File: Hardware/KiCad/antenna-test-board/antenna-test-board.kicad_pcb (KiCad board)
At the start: 2 copper layers, 50 x 80 mm, 3 parts, among them J1 50R

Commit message: chore(hardware): .kicad_pcb canonico, build reproducible byte a byte
Los UUID deterministas del commit anterior no bastaban: al guardar, KiCad
ordena footprints, pistas, vias y zonas con un criterio que acaba dependiendo
de sus KIID aleatorios, y reordena tambien los fp_text DENTRO de cada
footprint. El orden de los bloques cambiaba en cada build.

canonicalize() reordena los dos niveles por (tipo, texto sin UUID), que no
depende de nada aleatorio, preservando la indentacion que escribe KiCad. El
orden de los hijos de una s-expresion no tiene significado semantico, y
verify_board.py recarga el archivo y corre el DRC justo despues.

Comprobado con tres build.sh seguidos: mismo MD5 del .kicad_pcb las tres
veces, y DRC sigue en 0. Ahora un diff en un fichero generado significa un
cambio real de geometria.

Co-Authored-By: Claude Opus 5 <noreply@anthropic.com>
Claude-Session: https://claude.ai/code/session_01MCMeByymMLU6SJT81sefdN
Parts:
- removed the C101 at (39.2, 26.4)
- added J1: 50R, 0G_RF:TP_Coax_50R_NanoVNA, F.Cu at (39.2, 30.5)
- C101: renamed from J1; value 50R -> 2.2pF; footprint 0G_RF:TP_Coax_50R_NanoVNA -> 0G_RF:C_0402_1005Metric_0G
- moved C101 4.09 mm to (39.2, 26.4), turned to -90 degrees
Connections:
- C101 pad 1: GND -> ANT_FEED

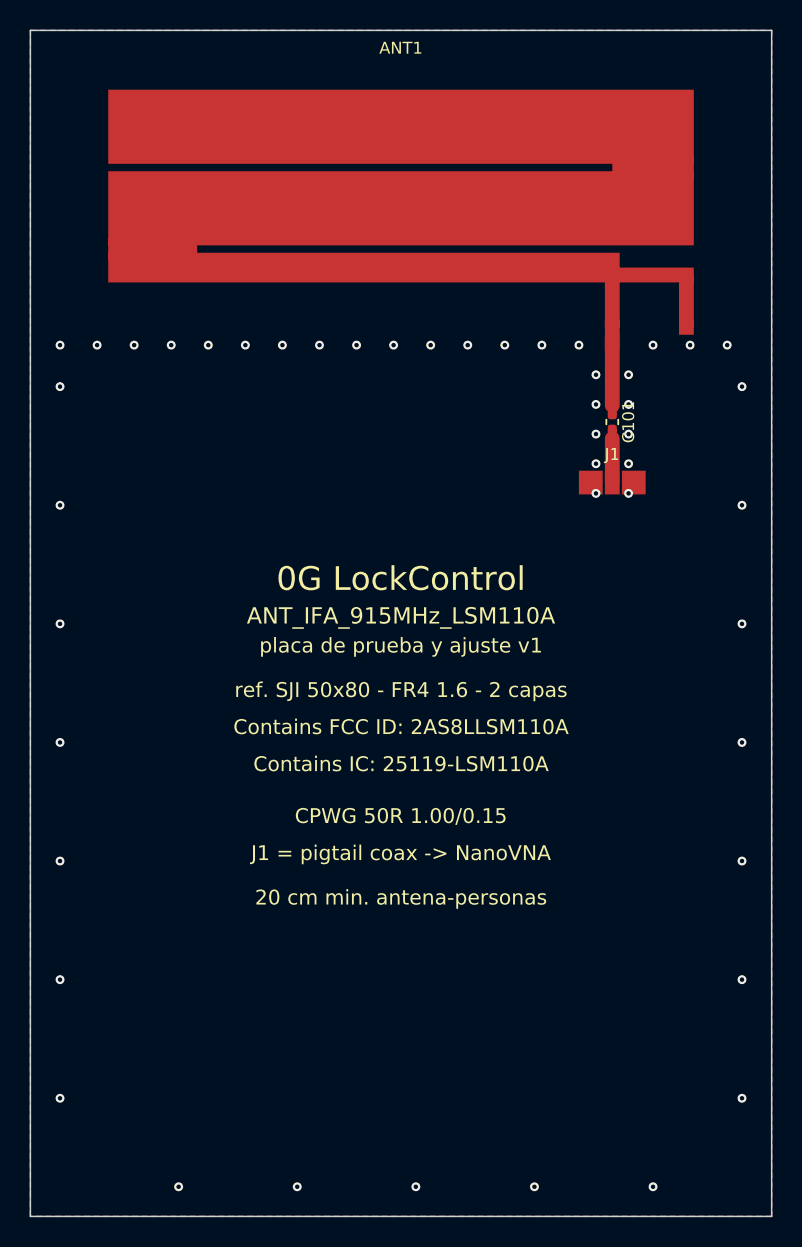
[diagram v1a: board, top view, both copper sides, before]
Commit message: feat(hardware): red de matching en PI segun la figura EVM LSM de SJI
La figura de la placa de evaluacion muestra junto al feed de la antena cuatro
designadores: CON101 (conector RF), L101, C101 y C102. O sea que la referencia
no lleva un condensador suelto en serie, lleva una red en PI con una posicion
serie y dos shunt. Eso resuelve la discrepancia que quedaba abierta entre el
plano ('C101 en serie') y certificacion-FCC/README.md ('C101 shunt'): las dos
fuentes describen la misma red, el plano la resume por un componente.

La placa de prueba pasa a montar las tres posiciones, con la poblacion de
referencia del User Manual FCC como valores por defecto (L101 = 0R, C101 =
2.2 pF, C102 = DNI). Asi se puede realizar cualquier topologia al ajustar
-serie sola, L, PI- sin rehacer la placa.

Detalles de layout que importan en RF:
- El pad interior de cada shunt monta SOBRE la linea (0.45 mm de solape). Con
  un muñon de 1 o 2 mm su inductancia serie arruinaria justo lo que el
  condensador tiene que hacer.
- Cada pad de GND de shunt lleva una via de retorno pegada (0.00 mm).
- La costura de vias esquiva los footprints: una via sobre un pad de GND no
  daria error de DRC (misma red), quedaria sin marcar y mal.
- El componente serie queda donde el plano pone la cota de 5.60.

Cotejo independiente de la geometria contra la misma figura, escalando por el
contorno de 50 x 80 mm del User Manual: las siete cotas medibles cuadran, y el
lado corto de la antena sale a 13.01 mm frente a los 13.00 de la
reconstruccion. La figura corrobora tambien la fila de ranuras mecanicas
(18.5 mm del borde, 1.95 de ancho), que pasa de 'sin verificar' a 'real pero
sin cotar': se mantiene en footprint aparte porque lo que falta es su cota.

Verificacion: 122 comprobaciones (17 + 63 + 42), 0 fallos, DRC en 0. Dos
errores nuevos encontrados y corregidos: serigrafias de C102 y J1 solapadas, y
el punto de sondeo del gap coplanar que caia sobre un pad de C101 y media
0.276 en vez de 0.15.

Queda abierto: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
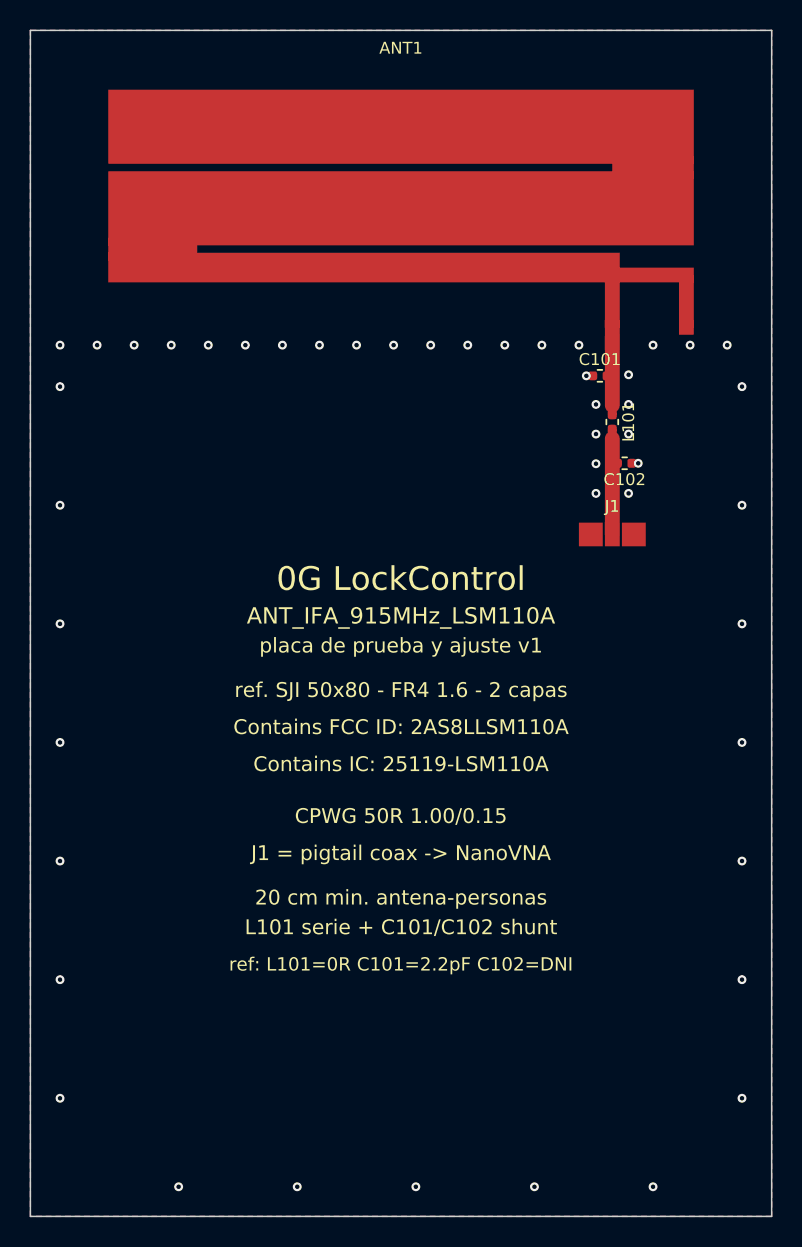
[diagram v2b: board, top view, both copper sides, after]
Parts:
- added C102: DNI, 0G_RF:C_0402_1005Metric_0G, F.Cu at (40.1, 29.2)
- added J1: 50R, 0G_RF:TP_Coax_50R_NanoVNA, F.Cu at (39.2, 34.0)
- L101: renamed from J1; value 50R -> 0R; footprint 0G_RF:TP_Coax_50R_NanoVNA -> 0G_RF:C_0402_1005Metric_0G
- moved L101 4.09 mm to (39.2, 26.4), turned to -90 degrees
- moved C101 3.22 mm to (38.4, 23.3), turned to 0 degrees
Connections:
- C101 pad 1: ANT_FEED -> GND
- C101 pad 2: RF_IN -> ANT_FEED
- L101 pad 1: GND -> ANT_FEED
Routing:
- net RF_IN: track 3.60 -> 7.10 mm
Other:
- board text added: "L101 serie + C101/C102 shunt"
- board text added: "ref: L101=0R C101=2.2pF C102=DNI"
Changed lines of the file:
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@@
+)
+  (footprint "0G_RF:C_0402_1005Metric_0G" (layer "F.Cu")
+    (at 38.415 23.3)
+    (descr "Condensador 0402 (1005 metrico), land IPC nominal: 2 pads de 0.60 x 0.60 mm a +/-0.485 mm. Definido en el proyecto para no depender de las bibliotecas estandar de KiCad. Uso previsto: C101, condensador serie de acoplo/matching en la linea RF de la antena.")
+    (tags "capacitor 0402 1005 RF matching")
+    (attr smd)
+    (fp_text reference "C101" (at 0 -1.1) (layer "F.SilkS")
+        (effects (font (size 0.8 0.8) (thickness 0.12)))
+    )
+    (fp_text user "${REFERENCE}" (at 0 0) (layer "F.Fab")
+        (effects (font (size 0.4 0.4) (thickness 0.06)))
+    )
+    (fp_text value "2.2pF" (at 0 1.1) (layer "F.Fab")
+        (effects (font (size 0.6 0.6) (thickness 0.1)))
+    )
+    (fp_line (start -0.16 -0.4) (end 0.16 -0.4)
+      (stroke (width 0.12) (type default)) (layer "F.SilkS"))
+    (fp_line (start -0.16 0.4) (end 0.16 0.4)
+      (stroke (width 0.12) (type default)) (layer "F.SilkS"))
+    (fp_rect (start -0.5 -0.25) (end 0.5 0.25)
+      (stroke (width 0.05) (type default)) (fill none) (layer "F.Fab"))
+    (fp_rect (start -0.91 -0.51) (end 0.91 0.51)
+      (stroke (width 0.05) (type default)) (fill none) (layer "F.CrtYd"))
+    (pad "1" smd roundrect (at -0.485 0) (size 0.6 0.6) (layers "F.Cu" "F.Paste" "F.Mask") (roundrect_rratio 0.25)
+      (net 1 "GND"))
+    (pad "2" smd roundrect (at 0.485 0) (size 0.6 0.6) (layers "F.Cu" "F.Paste" "F.Mask") (roundrect_rratio 0.25)
+      (net 2 "ANT_FEED"))
 )
   (footprint "0G_RF:C_0402_1005Metric_0G" (layer "F.Cu")
@@
     (tags "capacitor 0402 1005 RF matching")
     (attr smd)
-    (fp_text reference "C101" (at 0 -1.1 -90) (layer "F.SilkS")
+    (fp_text reference "L101" (at 0 -1.1 -90) (layer "F.SilkS")
         (effects (font (size 0.8 0.8) (thickness 0.12)))
     )
@@
         (effects (font (size 0.4 0.4) (thickness 0.06)))
     )
-    (fp_text value "2.2pF" (at 0 1.1 -90) (layer "F.Fab")
+    (fp_text value "0R" (at 0 1.1 -90) (layer "F.Fab")
         (effects (font (size 0.6 0.6) (thickness 0.1)))
     )
@@
       (net 3 "RF_IN"))
 )
+  (footprint "0G_RF:C_0402_1005Metric_0G" (layer "F.Cu")
+    (at 40.085 29.2 180)
+    (descr "Condensador 0402 (1005 metrico), land IPC nominal: 2 pads de 0.60 x 0.60 mm a +/-0.485 mm. Definido en el proyecto para no depender de las bibliotecas estandar de KiCad. Uso previsto: C101, condensador serie de acoplo/matching en la linea RF de la antena.")
+    (tags "capacitor 0402 1005 RF matching")
+    (attr smd)
+    (fp_text reference "C102" (at 0 -1.1 180) (layer "F.SilkS")
+        (effects (font (size 0.8 0.8) (thickness 0.12)))
+    )
+    (fp_text user "${REFERENCE}" (at 0 0 180) (layer "F.Fab")
+        (effects (font (size 0.4 0.4) (thickness 0.06)))
+    )
+    (fp_text value "DNI" (at 0 1.1 180) (layer "F.Fab")
+        (effects (font (size 0.6 0.6) (thickness 0.1)))
+    )
+    (fp_line (start -0.16 -0.4) (end 0.16 -0.4)
+      (stroke (width 0.12) (type default)) (layer "F.SilkS"))
+    (fp_line (start -0.16 0.4) (end 0.16 0.4)
+      (stroke (width 0.12) (type default)) (layer "F.SilkS"))
+    (fp_rect (start -0.5 -0.25) (end 0.5 0.25)
+      (stroke (width 0.05) (type default)) (fill none) (layer "F.Fab"))
+    (fp_rect (start -0.91 -0.51) (end 0.91 0.51)
+      (stroke (width 0.05) (type default)) (fill none) (layer "F.CrtYd"))
+    (pad "1" smd roundrect (at -0.485 0 180) (size 0.6 0.6) (layers "F.Cu" "F.Paste" "F.Mask") (roundrect_rratio 0.25)
+      (net 1 "GND"))
+    (pad "2" smd roundrect (at 0.485 0 180) (size 0.6 0.6) (layers "F.Cu" "F.Paste" "F.Mask") (roundrect_rratio 0.25)
+      (net 3 "RF_IN"))
+)
   (footprint "0G_RF:TP_Coax_50R_NanoVNA" (layer "F.Cu")
-    (at 39.25 30.5)
+    (at 39.25 34)
     (descr "Isla de 3 pads para soldar un pigtail coaxial de 50 ohm (RG-178 o semirrigido) y medir S11 con NanoVNA. Pad 1 = malla/GND izquierda, pad 2 = vivo, pad 3 = malla/GND derecha. La separacion vivo-malla es 0.15 mm, la misma del CPWG, para no crear discontinuidad. Solo para la placa de prueba y ajuste: no va en el producto.")
     (tags "coax test point NanoVNA S11 RF 50ohm")
@@
     (effects (font (size 1 1) (thickness 0.15)))
   )
+  (gr_text "L101 serie + C101/C102 shunt" (at 25 60.5) (layer "F.SilkS")
+    (effects (font (size 1 1) (thickness 0.15)))
+  )
   (gr_text "generado de antenna_geometry.py" (at 25 64) (layer "F.Fab")
     (effects (font (size 1 1) (thickness 0.15)))
@@
     (effects (font (size 1 1) (thickness 0.15)))
   )
+  (gr_text "ref: L101=0R C101=2.2pF C102=DNI" (at 25 63) (layer "F.SilkS")
+    (effects (font (size 0.9 0.9) (thickness 0.14)))
+  )
   (segment (start 39.25 20.63) (end 39.25 25.3) (width 1) (layer "F.Cu") (net 2))
   (segment (start 39.25 25.3) (end 39.25 25.93) (width 0.6) (layer "F.Cu") (net 2))
   (segment (start 39.25 26.9) (end 39.25 27.53) (width 0.6) (layer "F.Cu") (net 3))
-  (segment (start 39.25 27.53) (end 39.25 30.5) (width 1) (layer "F.Cu") (net 3))
+  (segment (start 39.25 27.53) (end 39.25 34) (width 1) (layer "F.Cu") (net 3))
   (via (at 10 78) (size 0.6) (drill 0.3) (layers "F.Cu" "B.Cu") (net 1))
   (via (at 12 21.23) (size 0.6) (drill 0.3) (layers "F.Cu" "B.Cu") (net 1))
@@
   (via (at 34.5 21.23) (size 0.6) (drill 0.3) (layers "F.Cu" "B.Cu") (net 1))
   (via (at 37 21.23) (size 0.6) (drill 0.3) (layers "F.Cu" "B.Cu") (net 1))
-  (via (at 38.15 23.23) (size 0.6) (drill 0.3) (layers "F.Cu" "B.Cu") (net 1))
+  (via (at 37.5 23.3) (size 0.6) (drill 0.3) (layers "F.Cu" "B.Cu") (net 1))
   (via (at 38.15 25.23) (size 0.6) (drill 0.3) (layers "F.Cu" "B.Cu") (net 1))
   (via (at 38.15 27.23) (size 0.6) (drill 0.3) (layers "F.Cu" "B.Cu") (net 1))
@@
   (via (at 40.35 25.23) (size 0.6) (drill 0.3) (layers "F.Cu" "B.Cu") (net 1))
   (via (at 40.35 27.23) (size 0.6) (drill 0.3) (layers "F.Cu" "B.Cu") (net 1))
-  (via (at 40.35 29.23) (size 0.6) (drill 0.3) (layers "F.Cu" "B.Cu") (net 1))
   (via (at 40.35 31.23) (size 0.6) (drill 0.3) (layers "F.Cu" "B.Cu") (net 1))
+  (via (at 41 29.2) (size 0.6) (drill 0.3) (layers "F.Cu" "B.Cu") (net 1))
   (via (at 42 21.23) (size 0.6) (drill 0.3) (layers "F.Cu" "B.Cu") (net 1))
   (via (at 42 78) (size 0.6) (drill 0.3) (layers "F.Cu" "B.Cu") (net 1))
